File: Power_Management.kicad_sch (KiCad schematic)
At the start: 38 parts

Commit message: Updated notes
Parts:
- R40: value 546R -> 480R
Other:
- note added: "TPS259531DSGR OUTPUT VOLTAGE CLAMP: 5.7 V (typ) UNDERVOLTAGE LOCKOUT: Vsupply = VUVLO * (R1 + R2) / R2 ACTIVE CURRENT LIMITING: RILM = 2000/(ILIMIT - 0.04), for 4A RILM = 495Ohms"
- note removed: "TPS259531DSGR OUTPUT VOLTAGE CLAMP: 5.7 V (typ) UNDERVOLTAGE LOCKOUT: Vsupply = VUVLO * (R1 + R2) / R2"
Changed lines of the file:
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@@
 		)
 	)
-	(text "TPS259531DSGR\nOUTPUT VOLTAGE CLAMP: 5.7 V (typ)\nUNDERVOLTAGE LOCKOUT: Vsupply = VUVLO * (R1 + R2) / R2"
-		(exclude_from_sim no)
-		(at 231.902 66.548 0)
+	(text "TPS259531DSGR\nOUTPUT VOLTAGE CLAMP: 5.7 V (typ)\nUNDERVOLTAGE LOCKOUT: Vsupply = VUVLO * (R1 + R2) / R2\nACTIVE CURRENT LIMITING: RILM = 2000/(ILIMIT - 0.04), for 4A RILM = 495Ohms"
+		(exclude_from_sim no)
+		(at 201.168 72.136 0)
 		(effects
 			(font
@@
 			)
 		)
-		(property "Value" "546R"
+		(property "Value" "480R"
 			(at 245.872 58.674 0)
 			(effects

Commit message: SMA Update
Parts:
- C14: value 470u -> 1u
- R35: value 1u -> 47k
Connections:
- net PG renamed PG_OD
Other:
- note added: "PG OUT NOT USED"
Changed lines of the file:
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@@
 	)
 	(junction
+		(at 157.48 31.75)
+		(diameter 0)
+		(color 0 0 0 0)
+	)
+	(junction
 		(at 83.82 43.18)
 		(diameter 0)
@@
 	)
 	(junction
-		(at 157.48 31.75)
-		(diameter 0)
-		(color 0 0 0 0)
-	)
-	(junction
 		(at 195.58 31.75)
 		(diameter 0)
@@
 	(wire
 		(pts
-			(xy 209.55 93.98) (xy 198.12 93.98)
+			(xy 157.48 31.75) (xy 187.96 31.75)
 		)
 		(stroke
@@
 	(wire
 		(pts
-			(xy 157.48 39.37) (xy 157.48 31.75)
+			(xy 209.55 93.98) (xy 198.12 93.98)
 		)
 		(stroke
@@
 	(wire
 		(pts
-			(xy 157.48 31.75) (xy 147.32 31.75)
-		)
-		(stroke
-			(width 0)
-			(type default)
-		)
-	)
-	(wire
-		(pts
 			(xy 209.55 96.52) (xy 209.55 93.98)
 		)
@@
 	(wire
 		(pts
+			(xy 157.48 31.75) (xy 157.48 39.37)
+		)
+		(stroke
+			(width 0)
+			(type default)
+		)
+	)
+	(wire
+		(pts
 			(xy 63.5 93.98) (xy 73.66 93.98)
 		)
@@
 	(wire
 		(pts
-			(xy 157.48 31.75) (xy 187.96 31.75)
+			(xy 147.32 31.75) (xy 157.48 31.75)
 		)
 		(stroke
@@
 		)
 	)
+	(text "PG OUT NOT USED"
+		(exclude_from_sim no)
+		(at 139.954 56.642 0)
+		(effects
+			(font
+				(size 1 1)
+			)
+		)
+	)
 	(text "Cout NC (output capacitor)\nOn the next stage"
 		(exclude_from_sim no)
@@
 		)
 	)
-	(label "PG"
+	(label "PG_OD"
 		(at 129.54 54.61 0)
 		(fields_autoplaced yes)
@@
 			)
 		)
-		(property "Value" "1u"
+		(property "Value" "47k"
 			(at 160.274 47.244 0)
 			(effects
@@
 			)
 		)
-		(property "Value" "470u"
+		(property "Value" "1u"
 			(at 148.336 46.228 0)
 			(effects

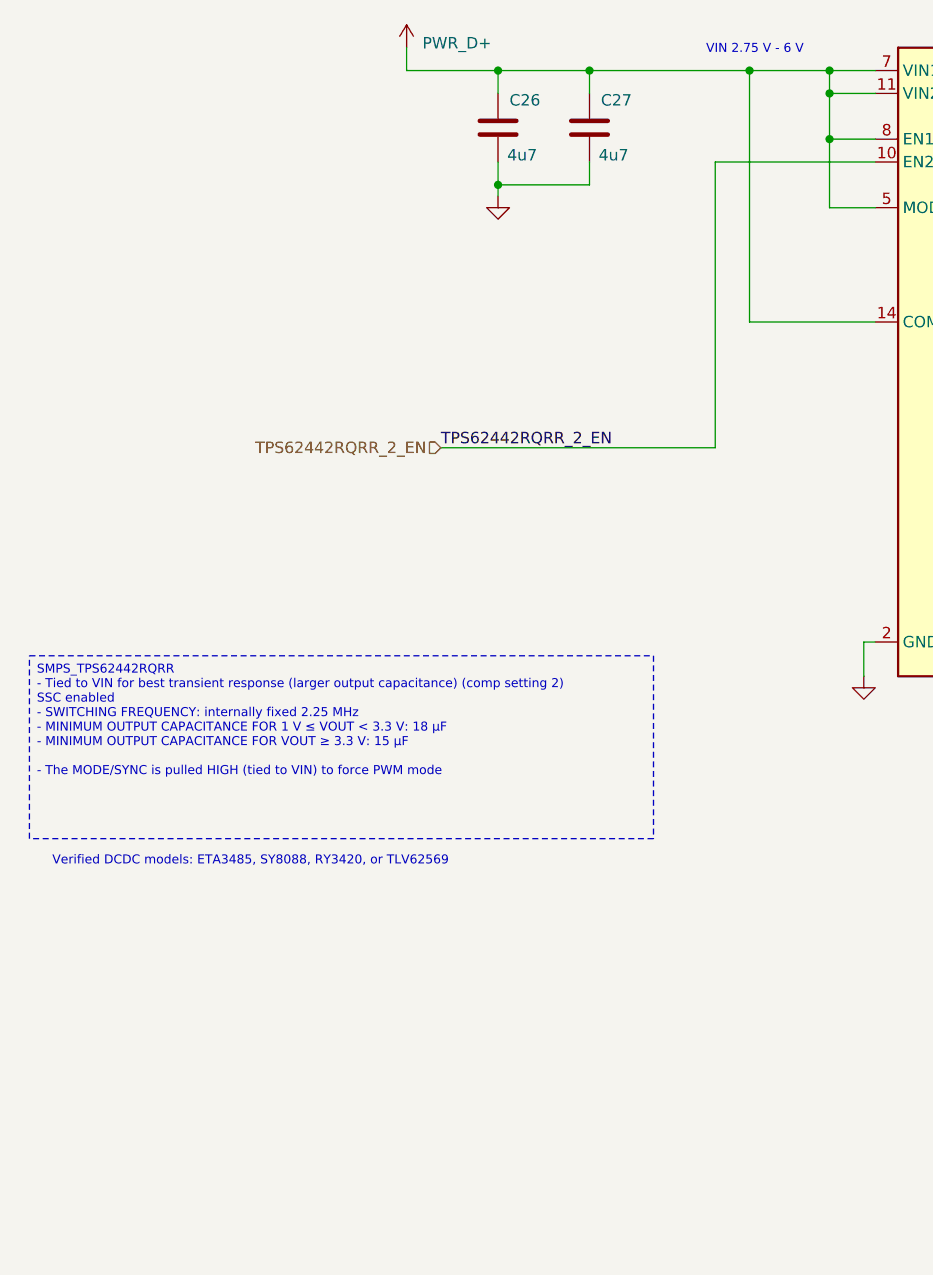
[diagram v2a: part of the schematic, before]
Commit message: QSPI Memory Bus
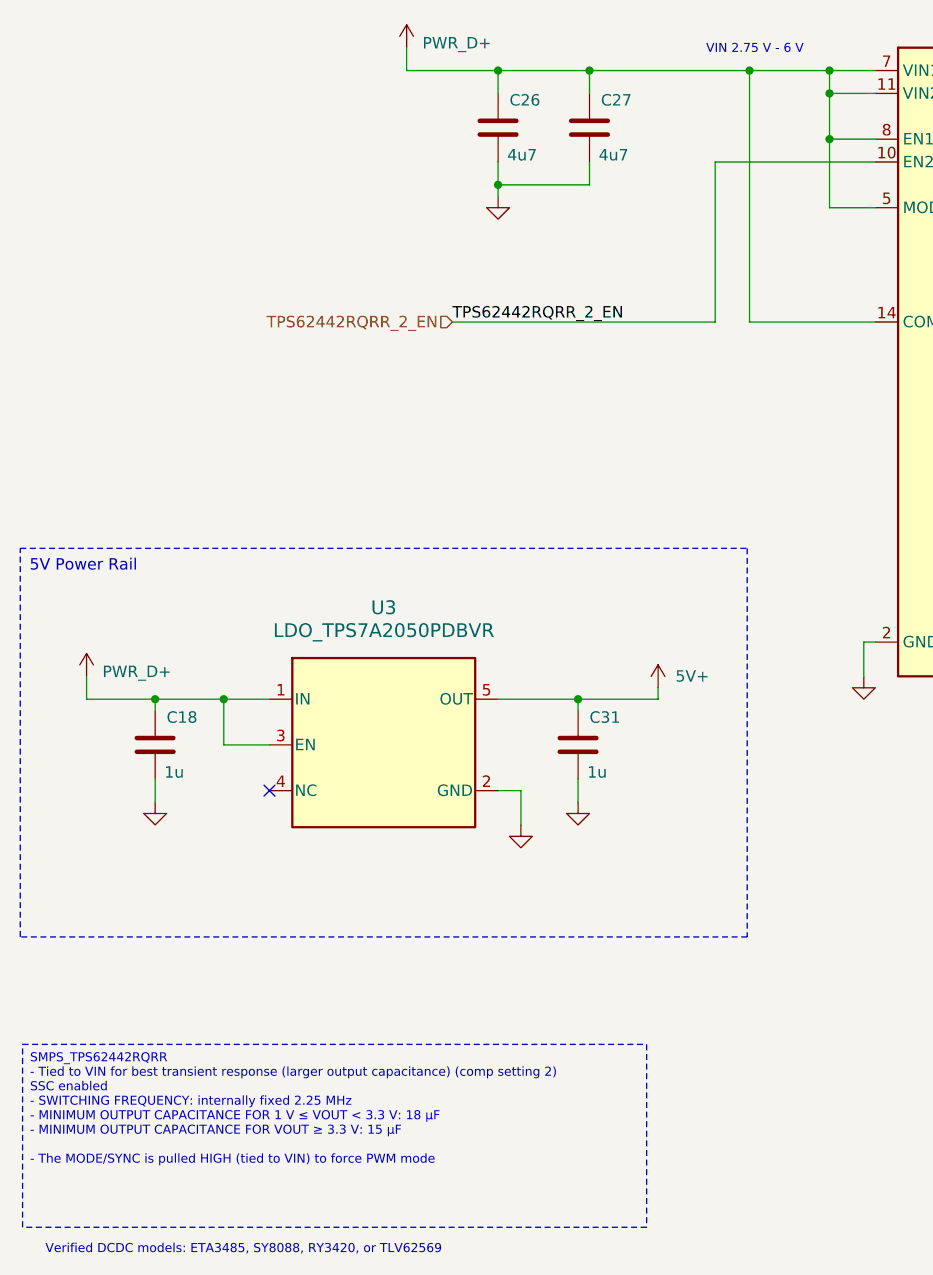
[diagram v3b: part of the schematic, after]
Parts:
- added C18, C31: 1u, Capacitor_SMD:C_0805_2012Metric, symbol Device:C
- added U3: LDO_TPS7A2050PDBVR, Personal_Project:LDO_TPS7A2050PDBVR, symbol Personal_Projects:LDO_TPS7A2050PDBVR
- C15: footprint Capacitor_SMD:C_0805_2012Metric -> Capacitor_SMD:C_0603_1608Metric
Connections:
- net GND: now also C18.1, C31.1, U3.2 (GND)
- net PWR_D+: now also C18.2, U3.1 (IN), U3.3 (EN)
- new net 5V+: C31.2, U3.5 (OUT)
- no-connect marks 0 -> 1

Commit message: Interface Update
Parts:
- added TP10, TP5, TP6, TP7, TP8, TP9: TestPoint, TestPoint:TestPoint_Pad_1.5x1.5mm, symbol Connector:TestPoint
- L1: footprint Inductor_SMD:L_1008_2520Metric -> l4
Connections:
- net 5V+: now also TP9.1
- net ESP_3V3: now also TP10.1, TP5.1
- net ESP_VDD_HP: now also TP6.1
- net PWR_C+: now also TP8.1
- net PWR_D+: now also TP7.1
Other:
- note added: "Verified DCDC models for ESP32P4: ETA3485, SY8088, RY3420, or TLV62569"
- note removed: "Verified DCDC models: ETA3485, SY8088, RY3420, or TLV62569"
- company: (none) -> Peter Hancak
- title: (none) -> ESP32P4C5_BOARD
- moved on the sheet: R46, R47

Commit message: Power rail update
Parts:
- removed R46, R47: 10k, Resistor_SMD:R_0805_2012Metric, symbol Device:R
- added D1: D_Zener_Small, symbol Device:D_Zener_Small
- C15: value 3n3 -> 10n
- R15: value 470k -> 464k
- R24: value 11k -> 33k2
- R25: value 47k -> 110k
- R32: value 549 -> 7k15
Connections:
- net GND: now also D1.2 (A)
- net IMON: now also D1.1 (K); no longer R32.1
- net PG1_TPS62442RQRR: no longer SMPS2.4 (PG1)
- net PG2_TPS62442RQRR: no longer names the net of SMPS2.13 (PG2)
- no-connect marks 1 -> 3
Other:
- note added: "FLT 6V MAX"
- moved on the sheet: R32, R39

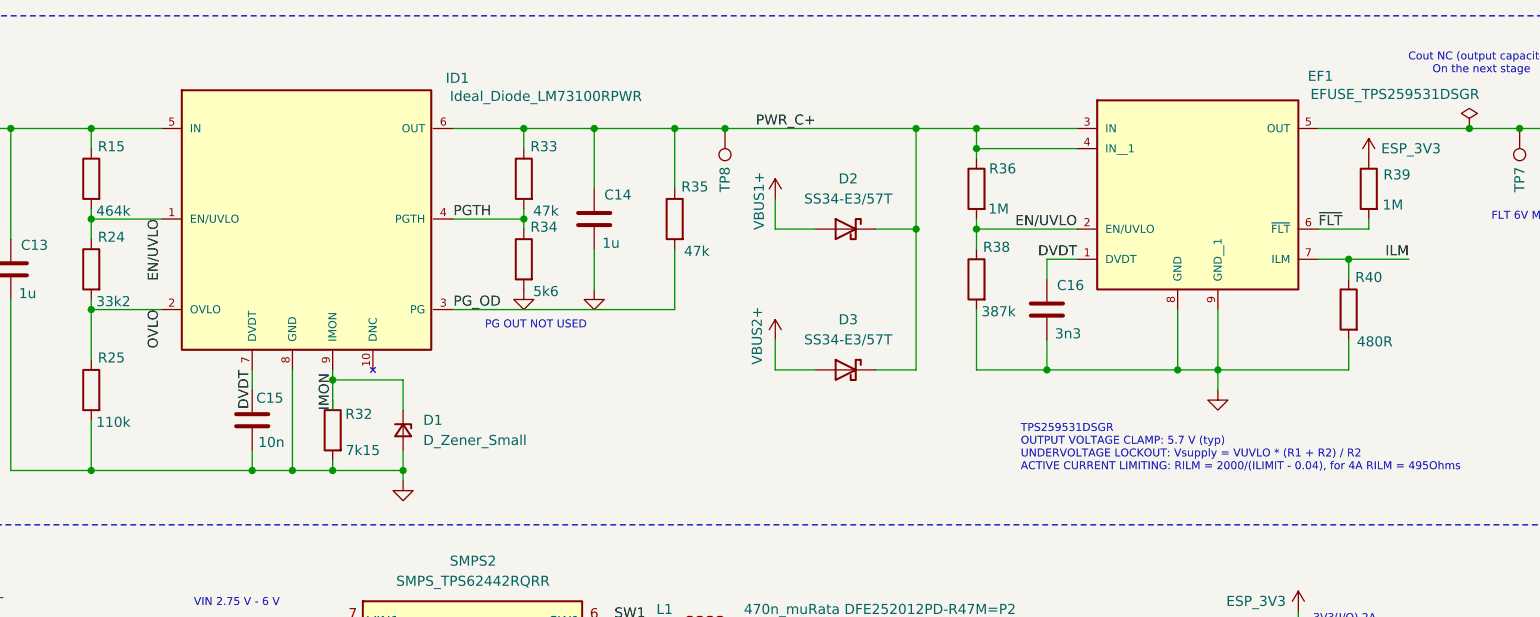
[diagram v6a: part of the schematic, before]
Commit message: Power Rail Update
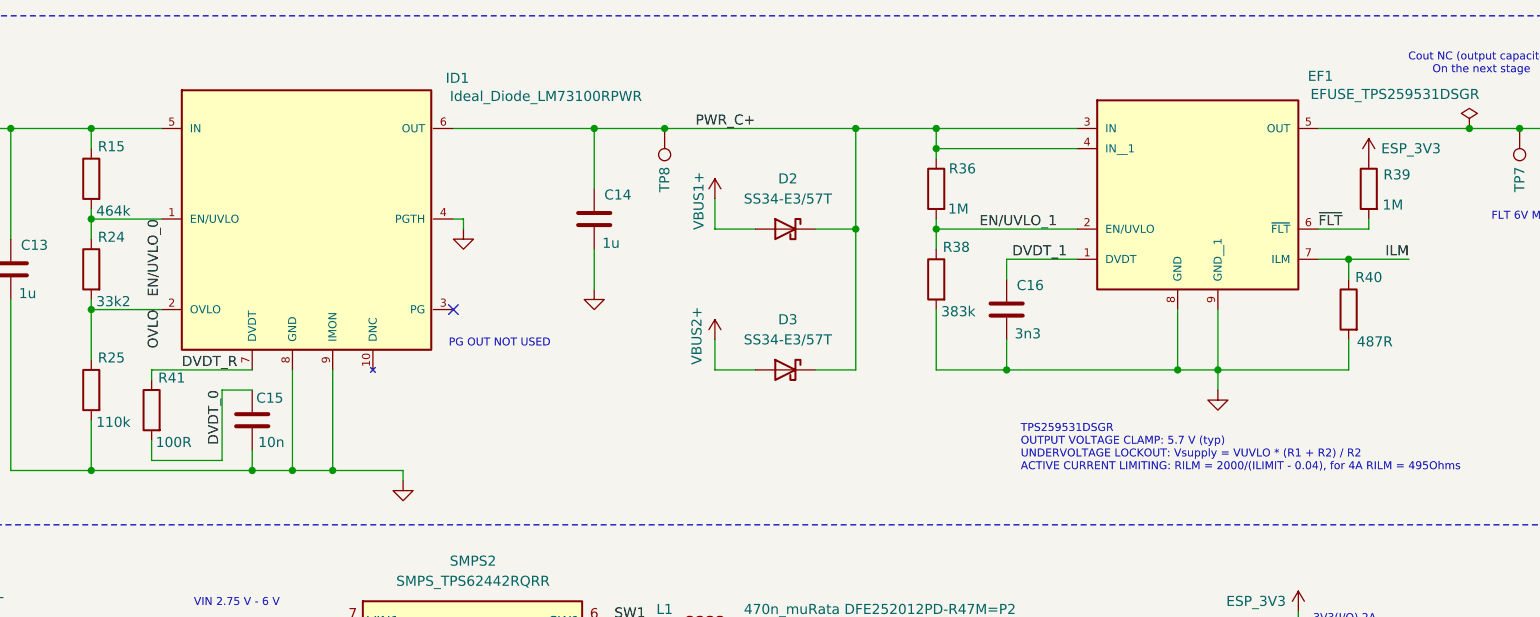
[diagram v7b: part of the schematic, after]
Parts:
- removed D1: D_Zener_Small, symbol Device:D_Zener_Small
- removed R32: 7k15, Resistor_SMD:R_0603_1608Metric, symbol Device:R
- removed R33: 47k, Resistor_SMD:R_0603_1608Metric, symbol Device:R
- removed R34: 5k6, Resistor_SMD:R_0603_1608Metric, symbol Device:R
- removed R35: 47k, Resistor_SMD:R_0805_2012Metric, symbol Device:R
- added R41: 100R, Resistor_SMD:R_0603_1608Metric, symbol Device:R
- R38: value 387k -> 383k
- R40: value 480R -> 487R
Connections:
- net IMON is gone; now on net GND: ID1.9 (IMON)
- net PGTH is gone; now on net GND: ID1.4 (PGTH)
- net DVDT renamed DVDT_1
- net DVDT_1: no longer C15.2, ID1.7 (DVDT)
- net EN/UVLO renamed EN/UVLO_0
- net EN/UVLO_0: no longer EF1.2 (EN/UVLO), R36.2, R38.1
- net PG_OD: no longer names the net of ID1.3 (PG)
- new net DVDT_0: C15.2, R41.2
- new net DVDT_R: ID1.7 (DVDT), R41.1
- new net EN/UVLO_1: EF1.2 (EN/UVLO), R36.2, R38.1
- no-connect marks 3 -> 4
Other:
- moved on the sheet: C16, D2, D3, R36, R38, TP8

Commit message: 5V SMPS
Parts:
- removed C18, C31: 1u, Capacitor_SMD:C_0805_2012Metric, symbol Device:C
- removed U3: LDO_TPS7A2050PDBVR, Personal_Project:LDO_TPS7A2050PDBVR, symbol Personal_Projects:LDO_TPS7A2050PDBVR
- added C40: 100n, Capacitor_SMD:C_0603_1608Metric, symbol Device:C
- added C42, C43, C44: 10u, Capacitor_SMD:C_0603_1608Metric, symbol Device:C
- added L3: 2u2_LPS3015-222MRC, Inductor_SMD:L_Coilcraft_LPS3010, symbol Device:L
- added R46: 100R, Resistor_SMD:R_0603_1608Metric, symbol Device:R
- added U6: SMPS_TPS63002DRCR, Personal_Projects:SMPS_TPS63002DRCR_10-VSON, symbol Personal_Components:SMPS_TPS63002DRCR
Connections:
- net 5V+: now also C43.2, C44.2, U6.1 (VOUT), U6.10 (FB)
- net GND: now also C40.1, C42.1, C43.1, C44.1, U6.11 (PAD), U6.3 (PGND), U6.9 (GND)
- net PWR_D+: now also C42.2, R46.1, U6.5 (VIN)
- new net L1: L3.1, U6.4 (L1)
- new net L2: L3.2, U6.2 (L2)
- new net VINA: C40.2, R46.2, U6.6 (EN), U6.7 (PS_SYNC), U6.8 (VINA)
- no-connect marks 4 -> 3
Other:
- moved on the sheet: C2, C21, C22, C23, C24, C25, C26, C27, L1, L2, R10, R43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
